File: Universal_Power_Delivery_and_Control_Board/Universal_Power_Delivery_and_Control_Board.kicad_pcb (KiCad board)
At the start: 2 copper layers, 97 parts, among them CN1 B03B-XASK-1-A(LF)(SN), CN2 B03B-XASK-1-A(LF)(SN), CN3 B03B-XASK-1-A(LF)(SN), CN4 B03B-XASK-1-A(LF)(SN), Q2 AO3401A, U1 TPS259470LRPWR, U10 SN74LVC1G17DCKR, U11 SN74LVC1G17DCKR, U12 SN74LVC1G17DCKR, U13 SN74LVC1G17DCKR, U14 SN74LVC1G17DCKR, U15 SN74LVC541APWR_C113281, U2 CH224Q_C46061833, U3 USBLC6-2SC6, U4 ESD2CAN24-ES, U5 S2B-ZR (LF)(SN), U6 USBLC6-2SC6, U7 TPS54202DDC, U8 TPS51385RJNR, U9 TPS24751RUVR

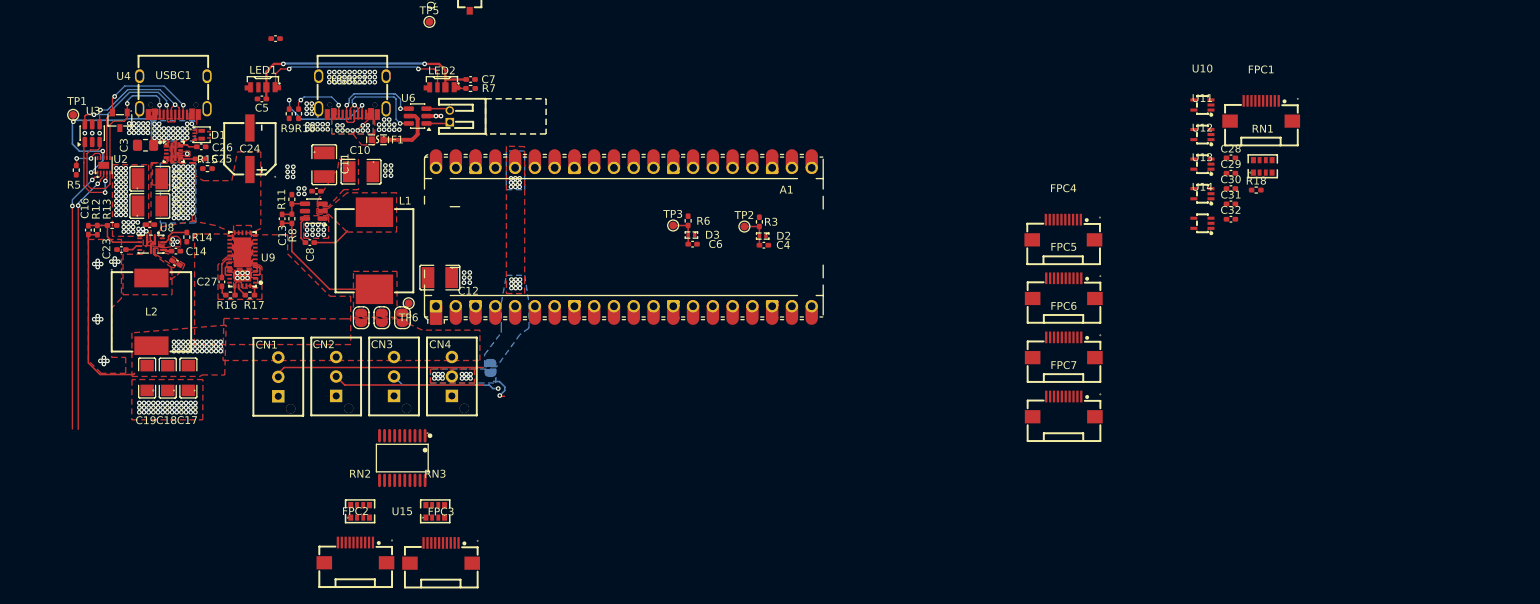
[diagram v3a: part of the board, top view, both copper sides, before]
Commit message: Switched to a 4 layer stackup and routed the digital output section.
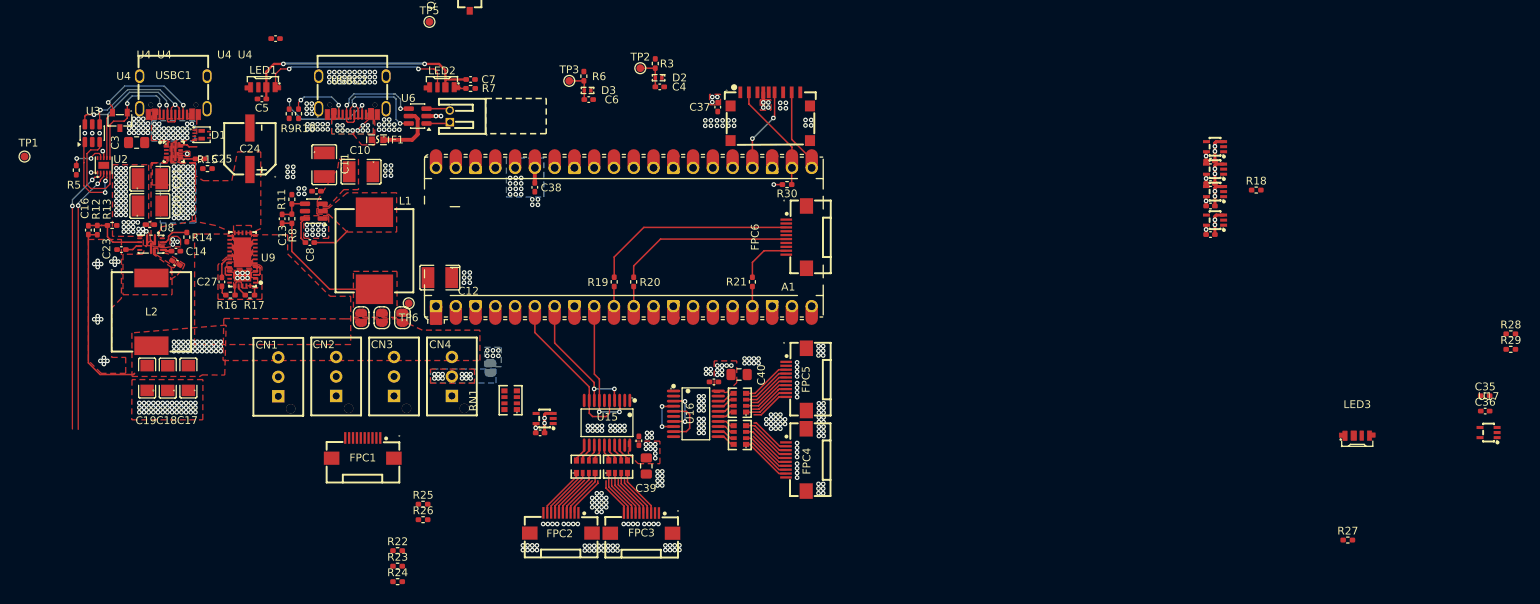
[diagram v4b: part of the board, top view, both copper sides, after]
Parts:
- removed C26: ?, Capacitor_SMD:C_0402_1005Metric_Pad0.74x0.62mm_HandSolder
- removed FPC7: XW05202-100R-00, lcsc_footprints:C2906114_FPC-SMD_10P-P0_50_HCTL_XW05202-100R-00
- added C33: 100nF, Capacitor_SMD:C_0402_1005Metric_Pad0.74x0.62mm_HandSolder, F.Cu at (175.9, 86.9)
- added C34: 100nF, Capacitor_SMD:C_0402_1005Metric_Pad0.74x0.62mm_HandSolder, F.Cu at (185.6, 79.3)
- added C35: 100nF, Capacitor_SMD:C_0402_1005Metric_Pad0.74x0.62mm_HandSolder, F.Cu at (284.6, 81.1)
- added C36: 100nF, Capacitor_SMD:C_0402_1005Metric_Pad0.74x0.62mm_HandSolder, F.Cu at (284.6, 83.1)
- added C37: 100nF, Capacitor_SMD:C_0402_1005Metric_Pad0.74x0.62mm_HandSolder, F.Cu at (186.1, 44.0)
- added C38: 100nF, Capacitor_SMD:C_0402_1005Metric_Pad0.74x0.62mm_HandSolder, F.Cu at (162.6, 54.4)
- added C39: 10uF, Capacitor_SMD:C_0805_2012Metric_Pad1.18x1.45mm_HandSolder, F.Cu at (176.9, 90.2)
- added C40: 10uF, Capacitor_SMD:C_0805_2012Metric_Pad1.18x1.45mm_HandSolder, F.Cu at (188.8, 78.4)
- added LED3: SK6812SIDE-A_C5378721, lcsc_footprints:C5378721_LED-SMD_4P-L4_0-W1_6-L, F.Cu at (268.2, 86.3)
- added R19: 33R, Resistor_SMD:R_0402_1005Metric_Pad0.72x0.64mm_HandSolder, F.Cu at (172.8, 66.5)
- added R20: 33R, Resistor_SMD:R_0402_1005Metric_Pad0.72x0.64mm_HandSolder, F.Cu at (175.2, 66.5)
- added R21: 33R, Resistor_SMD:R_0402_1005Metric_Pad0.72x0.64mm_HandSolder, F.Cu at (190.5, 66.5)
- added R22: 0R, Resistor_SMD:R_0402_1005Metric_Pad0.72x0.64mm_HandSolder, F.Cu at (144.9, 101.0)
- added R23: 0R, Resistor_SMD:R_0402_1005Metric_Pad0.72x0.64mm_HandSolder, F.Cu at (144.9, 103.0)
- added R24: 0R, Resistor_SMD:R_0402_1005Metric_Pad0.72x0.64mm_HandSolder, F.Cu at (144.9, 105.0)
- added R25: 0R, Resistor_SMD:R_0402_1005Metric_Pad0.72x0.64mm_HandSolder, F.Cu at (148.2, 95.1)
- added R26: 0R, Resistor_SMD:R_0402_1005Metric_Pad0.72x0.64mm_HandSolder, F.Cu at (148.2, 97.0)
- added R27: 10K, Resistor_SMD:R_0402_1005Metric_Pad0.72x0.64mm_HandSolder, F.Cu at (267.0, 99.7)
- added R28: 33R, Resistor_SMD:R_0402_1005Metric_Pad0.72x0.64mm_HandSolder, F.Cu at (287.9, 73.2)
- added R29: 470R, Resistor_SMD:R_0402_1005Metric_Pad0.72x0.64mm_HandSolder, F.Cu at (287.9, 75.2)
- added R30: 10K, Resistor_SMD:R_0402_1005Metric_Pad0.72x0.64mm_HandSolder, F.Cu at (194.9, 54.0)
- added RN4: 33R, lcsc_footprints:C165956_RES-ARRAY-SMD_0603-8P-L3_2-W1_6-BL, F.Cu at (188.9, 86.2)
- added RN5: 33R, lcsc_footprints:C165956_RES-ARRAY-SMD_0603-8P-L3_2-W1_6-BL, F.Cu at (188.9, 82.0)
- added U16: SN74LVC541APWR_C113281, lcsc_footprints:C113281_TSSOP-20_L6_5-W4_4-P0_65-LS6_4-BL, F.Cu at (183.2, 83.5)
- added U17: SN74LVC1G17DCKR, lcsc_footprints:C10425_SC-70-5_L2_1-W1_3-P0_65-LS2_1-BR, F.Cu at (285.1, 85.9)
- added U19: TF-0803-0, lcsc_footprints:C5362199_TF-SMD_XKTF-0803-0, F.Cu at (192.8, 45.2)
- RN2, RN3: value YC164-JR-0733RL -> 33R
- moved FPC1 123.3 mm to (140.4, 87.8)
- moved RN1 101.2 mm to (159.4, 81.7), turned to 90 degrees
- moved C28 95.5 mm to (163.2, 85.9)
- moved U10 93.6 mm to (163.8, 84.0)
- moved FPC4 45.3 mm to (196.1, 89.4), turned to 90 degrees
- moved FPC6 37.2 mm to (196.2, 60.8), turned to 90 degrees
- moved FPC5 36.3 mm to (196.1, 79.0), turned to 90 degrees
- moved RN2 29.6 mm to (169.1, 90.2)
- moved U15 26.7 mm to (171.8, 84.6)
- moved FPC2 26.7 mm to (165.9, 97.5)
- moved FPC3 26.0 mm to (176.2, 97.5)
- moved D2 24.3 mm to (178.4, 40.3)
- moved TP2 24.3 mm to (176.1, 39.0)
- moved C4 24.3 mm to (178.6, 41.5)
- moved R3 24.3 mm to (178.0, 38.5)
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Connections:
- A1 pad 10: unconnected-(A1-GPIO7-Pad10) -> Net-(A1-GPIO7)
- A1 pad 11: unconnected-(A1-GPIO8-Pad11) -> Net-(A1-GPIO8)
- A1 pad 12: unconnected-(A1-GPIO9-Pad12) -> /Digital_Signal_Output/D1
- A1 pad 14: unconnected-(A1-GPIO10-Pad14) -> /Digital_Signal_Output/D2
- A1 pad 15: unconnected-(A1-GPIO11-Pad15) -> /Digital_Signal_Output/D3
- A1 pad 16: unconnected-(A1-GPIO12-Pad16) -> /Digital_Signal_Output/D4
- A1 pad 17: unconnected-(A1-GPIO13-Pad17) -> Net-(A1-GPIO13)
- A1 pad 19: unconnected-(A1-GPIO14-Pad19) -> /Digital_Signal_Output/HIGH_CURRENT_EN
- A1 pad 20: unconnected-(A1-GPIO15-Pad20) -> /Digital_Signal_Output/OE_buffers
- A1 pad 21: unconnected-(A1-GPIO16-Pad21) -> /MISO
- A1 pad 22: unconnected-(A1-GPIO17-Pad22) -> /CS
- A1 pad 24: unconnected-(A1-GPIO18-Pad24) -> /SCK
- A1 pad 25: unconnected-(A1-GPIO19-Pad25) -> /MOSI
- A1 pad 32: unconnected-(A1-GPIO27_ADC1-Pad32) -> /PD_Section/CC1_read
- A1 pad 34: unconnected-(A1-GPIO28_ADC2-Pad34) -> /PD_Section/CC2_read
- A1 pad 35: unconnected-(A1-ADC_VREF-Pad35) -> +3V3
- A1 pad 6: unconnected-(A1-GPIO4-Pad6) -> /Digital_Signal_Output/CLK
- A1 pad 7: unconnected-(A1-GPIO5-Pad7) -> /Digital_Signal_Output/LE
- A1 pad 9: unconnected-(A1-GPIO6-Pad9) -> /Digital_Signal_Output/OE
- FPC2 pad 1: unconnected-(FPC2-Pad1) -> /Digital_Signal_Output/HIGH_CURRENT_EN
- FPC3 pad 1: unconnected-(FPC3-Pad1) -> /Digital_Signal_Output/HIGH_CURRENT_EN
- FPC4 pad 1: unconnected-(FPC4-Pad1) -> /Digital_Signal_Output/HIGH_CURRENT_EN
- FPC4 pad 3: unconnected-(FPC4-Pad3) -> Net-(FPC4-Pad3)
- FPC4 pad 5: unconnected-(FPC4-Pad5) -> Net-(FPC4-Pad5)
- FPC4 pad 7: unconnected-(FPC4-Pad7) -> Net-(FPC4-Pad7)
- FPC4 pad 9: unconnected-(FPC4-Pad9) -> Net-(FPC4-Pad9)
- FPC5 pad 1: unconnected-(FPC5-Pad1) -> /Digital_Signal_Output/HIGH_CURRENT_EN
- FPC5 pad 3: unconnected-(FPC5-Pad3) -> Net-(FPC5-Pad3)
- FPC5 pad 5: unconnected-(FPC5-Pad5) -> Net-(FPC5-Pad5)
- FPC5 pad 7: unconnected-(FPC5-Pad7) -> Net-(FPC5-Pad7)
- FPC5 pad 9: unconnected-(FPC5-Pad9) -> Net-(FPC5-Pad9)
- FPC6 pad 1: unconnected-(FPC6-Pad1) -> GND
- FPC6 pad 11: unconnected-(FPC6-Pad11) -> GND
- FPC6 pad 3: unconnected-(FPC6-Pad3) -> /Digital_Signal_Output/CLK_L
- FPC6 pad 5: unconnected-(FPC6-Pad5) -> GND
- FPC6 pad 6: GND -> /Digital_Signal_Output/DIN_L
- FPC6 pad 7: unconnected-(FPC6-Pad7) -> GND
- FPC6 pad 9: unconnected-(FPC6-Pad9) -> /Digital_Signal_Output/MR_L
- U1 pad 10: Net-(U1-ITIMER) -> unconnected-(U1-ITIMER-Pad10)
- U10 pad 2: /Power_Output/5V_O0 -> /Power_Output/5V_O1
- U11 pad 2: /Power_Output/5V_O1 -> /Power_Output/5V_O2
- U12 pad 2: /Power_Output/5V_O2 -> /Power_Output/5V_O3
- U13 pad 2: /Power_Output/5V_O3 -> /Power_Output/5V_O4
- U14 pad 2: /Power_Output/5V_O4 -> /Power_Output/5V_O5
- U15 pad 1: unconnected-(U15-OE1#-Pad1) -> /Digital_Signal_Output/OE_buffers
- U15 pad 19: unconnected-(U15-OE2#-Pad19) -> /Digital_Signal_Output/OE_buffers
- U15 pad 2: unconnected-(U15-A1-Pad2) -> /Digital_Signal_Output/D2
- U15 pad 3: Net-(U15-A2) -> /Digital_Signal_Output/OE
- U15 pad 4: Net-(U15-A3) -> /Digital_Signal_Output/LE
- U15 pad 5: Net-(U15-A4) -> /Digital_Signal_Output/CLK
- U15 pad 6: unconnected-(U15-A5-Pad6) -> /Digital_Signal_Output/D1
- U15 pad 7: Net-(U15-A2) -> /Digital_Signal_Output/OE
- U15 pad 8: Net-(U15-A3) -> /Digital_Signal_Output/LE
- U15 pad 9: Net-(U15-A4) -> /Digital_Signal_Output/CLK
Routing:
- net GND: track 5.04 -> 109.7 mm, vias 224 -> 441
- net Net-(CN1-Pad2): track 27.1 -> 0.00 mm
- net /Digital_Signal_Output/CLK: track 0.00 -> 26.7 mm
- net /Digital_Signal_Output/CLK_L: track 0.00 -> 26.3 mm
- net /Digital_Signal_Output/LE: track 0.00 -> 23.1 mm, vias 0 -> 4
- net /Digital_Signal_Output/OE: track 0.00 -> 22.7 mm, vias 0 -> 4
- net /PD_Section/PD_VBUS: track 24.9 -> 2.38 mm, vias 31 -> 30
- net /Digital_Signal_Output/DIN_L: track 0.00 -> 22.5 mm
- net Net-(CN2-Pad2): track 19.4 -> 0.00 mm
- net Net-(CN3-Pad2): track 14.0 -> 0.00 mm, vias 1 -> 0
- net /CS: track 0.00 -> 13.4 mm
- net /SCK: track 0.00 -> 10.1 mm, vias 0 -> 2
- net /MISO: track 0.00 -> 9.96 mm
- net /Digital_Signal_Output/MR_L: track 0.00 -> 6.87 mm
- net Net-(FPC4-Pad9): track 0.00 -> 6.67 mm
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- added copper zone on In2.Cu, net +3V3
- added copper zone on In2.Cu, net /PD_Section/PD_VBUS
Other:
- copper layers 2 -> 4
- board text added: "U4"

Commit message: Practically finshed the digital output layout, added the i2c io expander as im short on ios.
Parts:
- removed R22, R23, R24, R25, R26: 0R, Resistor_SMD:R_0402_1005Metric_Pad0.72x0.64mm_HandSolder
- added C41: 10uF, Capacitor_SMD:C_0805_2012Metric_Pad1.18x1.45mm_HandSolder, F.Cu at (163.5, 89.5)
- added C42: 100nF, Capacitor_SMD:C_0402_1005Metric_Pad0.74x0.62mm_HandSolder, F.Cu at (158.7, 67.5)
- added C43: 10uF, Capacitor_SMD:C_0805_2012Metric_Pad1.18x1.45mm_HandSolder, F.Cu at (168.6, 65.8)
- added G***: LOGO, LOGO, F.Cu at (79.9, 90.6)
- added JP5: SolderJumper_3_Bridged12, Jumper:SolderJumper-3_P1.3mm_Bridged12_Pad1.0x1.5mm_NumberLabels, F.Cu at (169.0, 59.0)
- added JP6: SolderJumper_3_Bridged12, Jumper:SolderJumper-3_P1.3mm_Bridged12_Pad1.0x1.5mm_NumberLabels, F.Cu at (169.0, 62.5)
- added U20: TCA9555PWR, Package_SO:TSSOP-24_4.4x7.8mm_P0.65mm, F.Cu at (162.4, 62.4)
- moved LED3 171.4 mm to (99.2, 114.6)
- moved R27 171.4 mm to (97.9, 128.0)
- moved R28 171.4 mm to (118.9, 101.5)
- moved R29 171.4 mm to (118.9, 103.5)
- moved C35 171.4 mm to (115.6, 109.5)
- moved C36 171.4 mm to (115.6, 111.4)
- moved U17 171.4 mm to (116.0, 114.2)
- moved R18 99.2 mm to (160.8, 84.9)
- moved U13 91.7 mm to (160.5, 75.3), turned to 45 degrees
- moved C32 91.6 mm to (161.7, 87.1), turned to 180 degrees
- moved U12 91.0 mm to (162.5, 77.3), turned to 45 degrees
- moved U11 90.6 mm to (164.5, 79.3), turned to 45 degrees
- moved U14 90.2 mm to (163.8, 85.6)
- moved C31 88.0 mm to (163.2, 74.8), turned to -45 degrees
- moved C30 87.3 mm to (165.1, 76.8), turned to -45 degrees
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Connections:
- A1 pad 1: unconnected-(A1-GPIO0-Pad1) -> /SCL
- A1 pad 10: Net-(A1-GPIO7) -> /Power_Output/5V_O4
- A1 pad 11: Net-(A1-GPIO8) -> /Power_Output/5V_O5
- A1 pad 2: unconnected-(A1-GPIO1-Pad2) -> /SDA
- A1 pad 39: unconnected-(A1-VSYS-Pad39) -> +5V_VSYS
- A1 pad 4: unconnected-(A1-GPIO2-Pad4) -> /INT
- A1 pad 6: /Digital_Signal_Output/CLK -> /Power_Output/5V_O1
- A1 pad 7: /Digital_Signal_Output/LE -> /Power_Output/5V_O2
- A1 pad 9: /Digital_Signal_Output/OE -> /Power_Output/5V_O3
- FPC1 pad 1: Net-(CN1-Pad2) -> Net-(FPC1-Pad1)
- FPC1 pad 3: Net-(CN2-Pad2) -> Net-(CN1-Pad2)
- FPC1 pad 5: Net-(CN3-Pad2) -> Net-(CN2-Pad2)
- FPC1 pad 7: Net-(JP4-B) -> Net-(CN3-Pad2)
- FPC1 pad 9: Net-(FPC1-Pad9) -> Net-(JP4-B)
- R18 pad 1: Net-(FPC1-Pad9) -> Net-(FPC1-Pad1)
- R19 pad 2: Net-(A1-GPIO7) -> /Power_Output/5V_O4
- R20 pad 2: Net-(A1-GPIO8) -> /Power_Output/5V_O5
- U15 pad 3: /Digital_Signal_Output/OE -> /Power_Output/5V_O3
- U15 pad 4: /Digital_Signal_Output/LE -> /Power_Output/5V_O2
- U15 pad 5: /Digital_Signal_Output/CLK -> /Power_Output/5V_O1
- U15 pad 7: /Digital_Signal_Output/OE -> /Power_Output/5V_O3
- U15 pad 8: /Digital_Signal_Output/LE -> /Power_Output/5V_O2
- U15 pad 9: /Digital_Signal_Output/CLK -> /Power_Output/5V_O1
- U16 pad 3: /Digital_Signal_Output/OE -> /Power_Output/5V_O3
- U16 pad 4: /Digital_Signal_Output/LE -> /Power_Output/5V_O2
- U16 pad 5: /Digital_Signal_Output/CLK -> /Power_Output/5V_O1
- U16 pad 7: /Digital_Signal_Output/OE -> /Power_Output/5V_O3
- U16 pad 8: /Digital_Signal_Output/LE -> /Power_Output/5V_O2
- U16 pad 9: /Digital_Signal_Output/CLK -> /Power_Output/5V_O1
- U2 pad 2: /PD_Section/SCL -> /SCL
- U2 pad 3: /PD_Section/SDA -> /SDA
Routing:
- net /Power_Output/PG_TPS51385: track 0.00 -> 52.5 mm, vias 0 -> 4
- net /Power_Output/MODE_TPS51385: track 0.00 -> 44.2 mm, vias 0 -> 3
- net Net-(CN1-Pad2): track 0.00 -> 43.3 mm, vias 0 -> 1
- net /Digital_Signal_Output/OE_buffers: track 0.00 -> 42.1 mm, vias 0 -> 5
- net /Power_Output/EN_TPS51385: track 3.90 -> 44.1 mm, vias 0 -> 3
- net /Power_Output/5V_O1: track 0.00 -> 38.6 mm
- net /Power_Output/5V_O3: track 0.00 -> 37.7 mm, vias 0 -> 6
- net +5V_VSYS: track 37.9 -> 1.50 mm, vias 7 -> 39
- net Net-(CN2-Pad2): track 0.00 -> 35.4 mm, vias 0 -> 1
- net /SCL: track 0.00 -> 34.8 mm, vias 0 -> 2
- net /PD_Section/SCL: track 34.8 -> 0.00 mm, vias 2 -> 0
- net /Power_Output/5V_O2: track 0.00 -> 34.5 mm, vias 0 -> 6
- net /SDA: track 0.00 -> 34.3 mm, vias 0 -> 2
- net /PD_Section/SDA: track 34.3 -> 0.00 mm, vias 2 -> 0
- net /Digital_Signal_Output/CLK: track 26.7 -> 0.00 mm
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- added copper zone on B.Cu, net +5V_VSYS
- added copper zone on F.Cu, net +5V_VSYS
- added copper zone on In2.Cu, net +5V_VSYS
- added copper zone on In1.Cu, net GND

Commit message: Added some misc stuff layout almost finished.
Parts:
- removed C12: 47uF, lcsc_footprints:C77101_C1210
- removed JP3: SolderJumper_2_Open, Jumper:SolderJumper-2_P1.3mm_Open_RoundedPad1.0x1.5mm
- removed Q2: AO3401A, lcsc_footprints:C15127_SOT-23_L2_9-W1_3-P1_90-LS2_4-BR
- removed R28: 33R, Resistor_SMD:R_0402_1005Metric_Pad0.72x0.64mm_HandSolder
- added C1: 1uF, Capacitor_SMD:C_0603_1608Metric_Pad1.08x0.95mm_HandSolder, F.Cu at (135.9, 47.3)
- added C26: 47uF, lcsc_footprints:C426659_C1206, F.Cu at (150.3, 66.5)
- added C44: 10nF, Capacitor_SMD:C_0402_1005Metric_Pad0.74x0.62mm_HandSolder, F.Cu at (150.7, 48.6)
- added JP10: SolderJumper_2_Open, Jumper:SolderJumper-2_P1.3mm_Open_RoundedPad1.0x1.5mm, F.Cu at (139.5, 53.6)
- added JP7: SolderJumper_2_Open, Jumper:SolderJumper-2_P1.3mm_Open_RoundedPad1.0x1.5mm, F.Cu at (150.1, 57.3)
- added JP8: SolderJumper_2_Open, Jumper:SolderJumper-2_P1.3mm_Open_RoundedPad1.0x1.5mm, F.Cu at (150.1, 54.8)
- added JP9: SolderJumper_2_Open, Jumper:SolderJumper-2_P1.3mm_Open_RoundedPad1.0x1.5mm, F.Cu at (139.5, 51.0)
- added R22: ?, Resistor_SMD:R_0402_1005Metric_Pad0.72x0.64mm_HandSolder, F.Cu at (121.0, 52.9)
- added R23: 1K, Resistor_SMD:R_0402_1005Metric_Pad0.72x0.64mm_HandSolder, F.Cu at (148.5, 59.9)
- added R24: 1K, Resistor_SMD:R_0402_1005Metric_Pad0.72x0.64mm_HandSolder, F.Cu at (148.3, 48.6)
- added R25: 4.7K, Resistor_SMD:R_0402_1005Metric_Pad0.72x0.64mm_HandSolder, F.Cu at (156.4, 65.9)
- added R26: 4.7K, Resistor_SMD:R_0402_1005Metric_Pad0.72x0.64mm_HandSolder, F.Cu at (155.1, 65.9)
- added REF**: OSHW-Logo2_14.6x12mm_SilkScreen, Symbol:OSHW-Logo2_14.6x12mm_SilkScreen, F.Cu at (144.3, 97.7)
- added REF**: ESD-Logo_13.2x12mm_SilkScreen, Symbol:ESD-Logo_13.2x12mm_SilkScreen, F.Cu at (129.5, 96.3)
- added SW2: TS1102-TD35HBM, lcsc_footprints:C36936640_SW-SMD_TS1102-TD35HBM, F.Cu at (108.5, 101.9)
- added U18: LM66200DRLR, lcsc_footprints:C3235556_SOT-583-8_L2_1-W1_2-P0_50-LS1_6-BL, F.Cu at (150.3, 59.9)
- added U21: TPS22919DCK, Package_TO_SOT_SMD:SOT-363_SC-70-6, F.Cu at (142.5, 51.0)
- added U22: HC-PM254-8.5H-2X4PW-02A, lcsc_footprints:C42163146_HDR-TH_8P-P2_54-H-F-R2-C4-S2_54-W8_5, F.Cu at (179.3, 47.0)
- F1: value 06H1100D -> Fuse; footprint lcsc_footprints:C182303_F0603 -> Fuse:Fuse_1206_3216Metric_Pad1.42x1.75mm_HandSolder
- JP4: moved to F.Cu
- R11, R15: value 13.3K -> ?
- R3, R6: value 1K -> 4.7K
- moved R27 104.0 mm to (187.8, 75.5), turned to 90 degrees
- moved G*** 76.6 mm to (155.1, 104.9)
- moved R3 47.2 mm to (131.0, 42.4), turned to 90 degrees
- moved R6 36.7 mm to (132.2, 42.4), turned to 90 degrees
- moved TP4 29.9 mm to (143.7, 54.3)
- moved C2 21.1 mm to (113.0, 48.8), turned to 180 degrees
- moved LED3 18.2 mm to (112.1, 101.8), turned to -90 degrees
- moved C4 16.3 mm to (169.6, 55.1), turned to 180 degrees
- moved D2 16.2 mm to (169.8, 53.9), turned to 0 degrees
- moved JP5 13.7 mm to (155.4, 57.1), turned to 90 degrees
- moved JP6 12.8 mm to (157.9, 56.1), turned to 90 degrees
- moved C6 12.7 mm to (165.7, 55.1)
- moved D3 12.7 mm to (165.5, 54.0)
- moved C42 11.1 mm to (164.4, 58.0), turned to 180 degrees
- moved TP2 10.9 mm to (170.2, 48.2)
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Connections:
- net /Power_Output/5V_O1 renamed /Digital_Signal_Output/CLK
- net /Power_Output/5V_O2 renamed /Digital_Signal_Output/LE
- net /Power_Output/5V_O3 renamed /Digital_Signal_Output/OE
- A1 pad 1: /SCL -> /SDA
- A1 pad 2: /SDA -> /SCL
- A1 pad 5: unconnected-(A1-GPIO3-Pad5) -> /SS_EN
- C10 pad 2: Net-(U7-VIN) -> +12V_PD
- C11 pad 2: Net-(U7-VIN) -> +12V_PD
- C9 pad 1: Net-(U7-VIN) -> +12V_PD
- CN1 pad : (no net) -> GND
- CN2 pad : (no net) -> GND
- CN3 pad : (no net) -> GND
- CN4 pad : (no net) -> GND
- F1 pad 1: +5V_VBUS -> /PD_Section/VBUS
- F1 pad 2: Net-(F1-Pad2) -> Net-(U21-IN)
- R15 pad 2: unconnected-(R15-Pad2) -> Net-(R15-Pad2)
- R17 pad 1: /Power_Output/SOFT_START_EN -> /SS_EN
- R29 pad 1: Net-(R28-Pad2) -> Net-(U17-Y)
- TP4 pad 1: +5V_VBUS -> /PD_Section/VBUS
- U20 pad 13: unconnected-(U20-P10-Pad13) -> Net-(U20-P10)
- U20 pad 14: unconnected-(U20-P11-Pad14) -> Net-(U20-P11)
- U20 pad 15: unconnected-(U20-P12-Pad15) -> Net-(U20-P12)
- U20 pad 16: unconnected-(U20-P13-Pad16) -> Net-(U20-P13)
- U20 pad 17: unconnected-(U20-P14-Pad17) -> Net-(U20-P14)
- U20 pad 18: unconnected-(U20-P15-Pad18) -> Net-(U20-P15)
- U20 pad 4: unconnected-(U20-P00-Pad4) -> /P00
- U20 pad 5: unconnected-(U20-P01-Pad5) -> /P01
- U20 pad 6: unconnected-(U20-P02-Pad6) -> /P02
- U20 pad 7: unconnected-(U20-P03-Pad7) -> /P03
- U20 pad 8: unconnected-(U20-P04-Pad8) -> /P04
- U20 pad 9: unconnected-(U20-P05-Pad9) -> /P05
- U6 pad 5: +5V_VBUS -> Net-(U21-IN)
- U7 pad 3: Net-(U7-VIN) -> +12V_PD
- U9 pad 33: /Power_Output/SOFT_START_EN -> /SS_EN
- USBC2 pad A4B9: Net-(F1-Pad2) -> Net-(U21-IN)
- USBC2 pad B4A9: Net-(F1-Pad2) -> Net-(U21-IN)
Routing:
- net /PD_Section/CC1_read: track 4.33 -> 53.6 mm, vias 0 -> 1
- net /PD_Section/CC2_read: track 4.33 -> 46.0 mm, vias 0 -> 1
- net /SS_EN: track 0.00 -> 41.5 mm, vias 0 -> 3
- net Net-(U20-P15): track 0.00 -> 31.2 mm
- net Net-(U20-P14): track 0.00 -> 29.3 mm, vias 0 -> 1
- net Net-(U20-P10): track 0.00 -> 27.6 mm
- net Net-(U20-P11): track 0.00 -> 25.5 mm
- net Net-(U20-P13): track 0.00 -> 24.6 mm
- net Net-(U20-P12): track 0.00 -> 23.6 mm
- net /INT: track 0.00 -> 16.5 mm, vias 0 -> 2
- net /SCL: track 34.8 -> 21.4 mm, vias 2 -> 1
- net Net-(U21-ON): track 0.00 -> 12.8 mm, vias 0 -> 2
- net GND: track 91.6 -> 102.2 mm, vias 457 -> 497
- net /SDA: track 34.3 -> 24.5 mm, vias 2 -> 3
- net Net-(U21-IN): track 0.00 -> 7.97 mm, vias 0 -> 28
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- added copper zone on F.Cu, net /PD_Section/VBUS
- added copper zone on B.Cu, net Net-(U21-IN)
- added copper zone on F.Cu, net Net-(U21-IN)
- removed copper zone on B.Cu, net Net-(F1-Pad2)
- removed copper zone on F.Cu, net Net-(F1-Pad2)
- removed copper zone on F.Cu, net Net-(U7-VIN)
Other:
- board outline added: 99.5 x 99.5 mm
